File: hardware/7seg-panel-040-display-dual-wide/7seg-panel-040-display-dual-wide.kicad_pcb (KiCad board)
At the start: 2 copper layers, 100 x 100 mm, 30 parts, among them J100 Conn_02x04_Odd_Even, J101 Conn_02x04_Odd_Even, J102 Conn_02x04_Odd_Even, J103 Conn_02x04_Odd_Even, J104 Conn_02x04_Odd_Even, J105 Conn_02x04_Odd_Even, U100 YH-2E20402-IK, U101 YH-2E20402-IK, U102 YH-2E20402-IK, U103 YH-2E20402-IK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

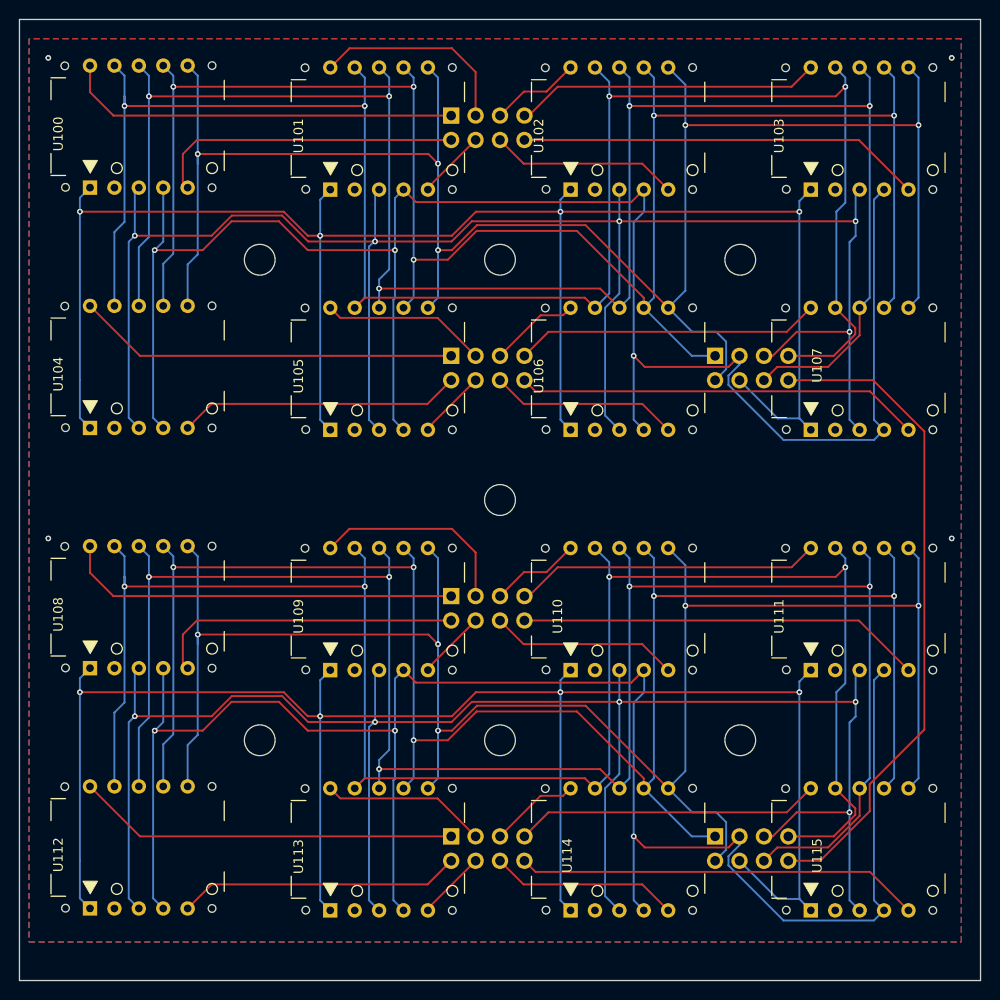
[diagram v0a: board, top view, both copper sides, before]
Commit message: hardware: KiCad ファイルの更新と不要ファイルの削除
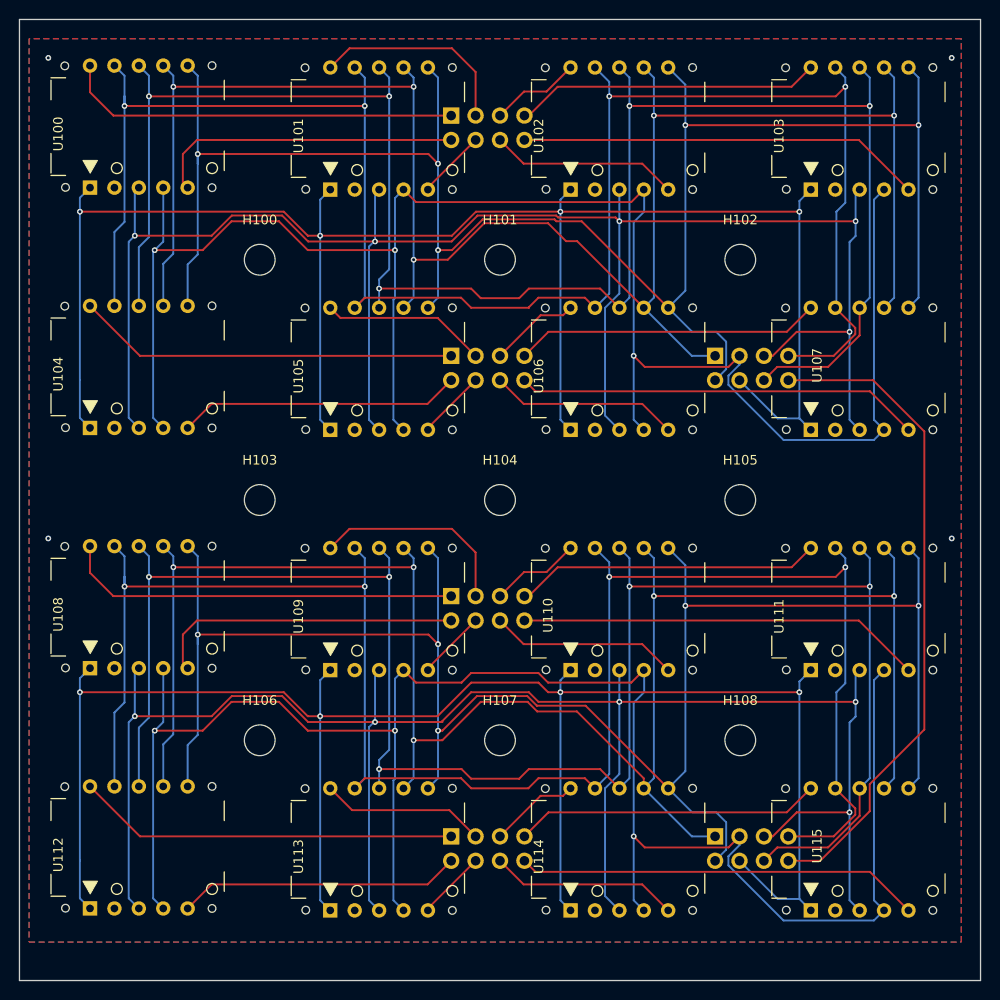
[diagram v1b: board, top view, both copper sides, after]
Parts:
- added H107: MountingHole, MountingHole:MountingHole_3.2mm_M3, F.Cu at (148.1, 145.2)
- added H108: MountingHole, MountingHole:MountingHole_3.2mm_M3, F.Cu at (173.1, 145.2)
- moved H106 50.0 mm to (123.1, 145.2)
- moved H104 35.4 mm to (148.1, 120.2)
- moved H105 35.4 mm to (173.1, 120.2), turned to 0 degrees
- moved H103 25.0 mm to (123.1, 120.2), turned to 0 degrees
- turned H101 to 0 degrees
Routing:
- net A_COM6: track 192.2 -> 193.1 mm
- net B_COM4: track 191.7 -> 192.6 mm
- net B_COM6: track 192.2 -> 193.1 mm
- net B_COM1: track 195.3 -> 196.2 mm
- net B_COM0: track 192.1 -> 192.9 mm
- net A_COM5: track 194.1 -> 194.9 mm
- net B_COM5: track 194.1 -> 194.9 mm
- net B_COM3: track 188.4 -> 189.2 mm
- net B_COM2: track 191.5 -> 192.4 mm
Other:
- board text added: "2026.03.23 << DIGITI >> 0.40{dblquote} panel dual sparse 2 channels; col 8 x row 4"
- board text removed: "2026.03.11 << DIGITI >> 0.40{dblquote} panel dual 2 channels; col 8 x row 4"
